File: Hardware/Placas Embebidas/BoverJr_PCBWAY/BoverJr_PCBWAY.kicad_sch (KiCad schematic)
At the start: 38 parts, among them J3 Encoder Derecho, J3 Programador, J4 Encoder Izquierdo, J5 Distancia_Der, J6 Distancia_Izq, J7 Distancia_Frontal, J8 7.4v, SW1 SW_Push, SW1 SW_SPDT, U1 ESP32-WROOM-32E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

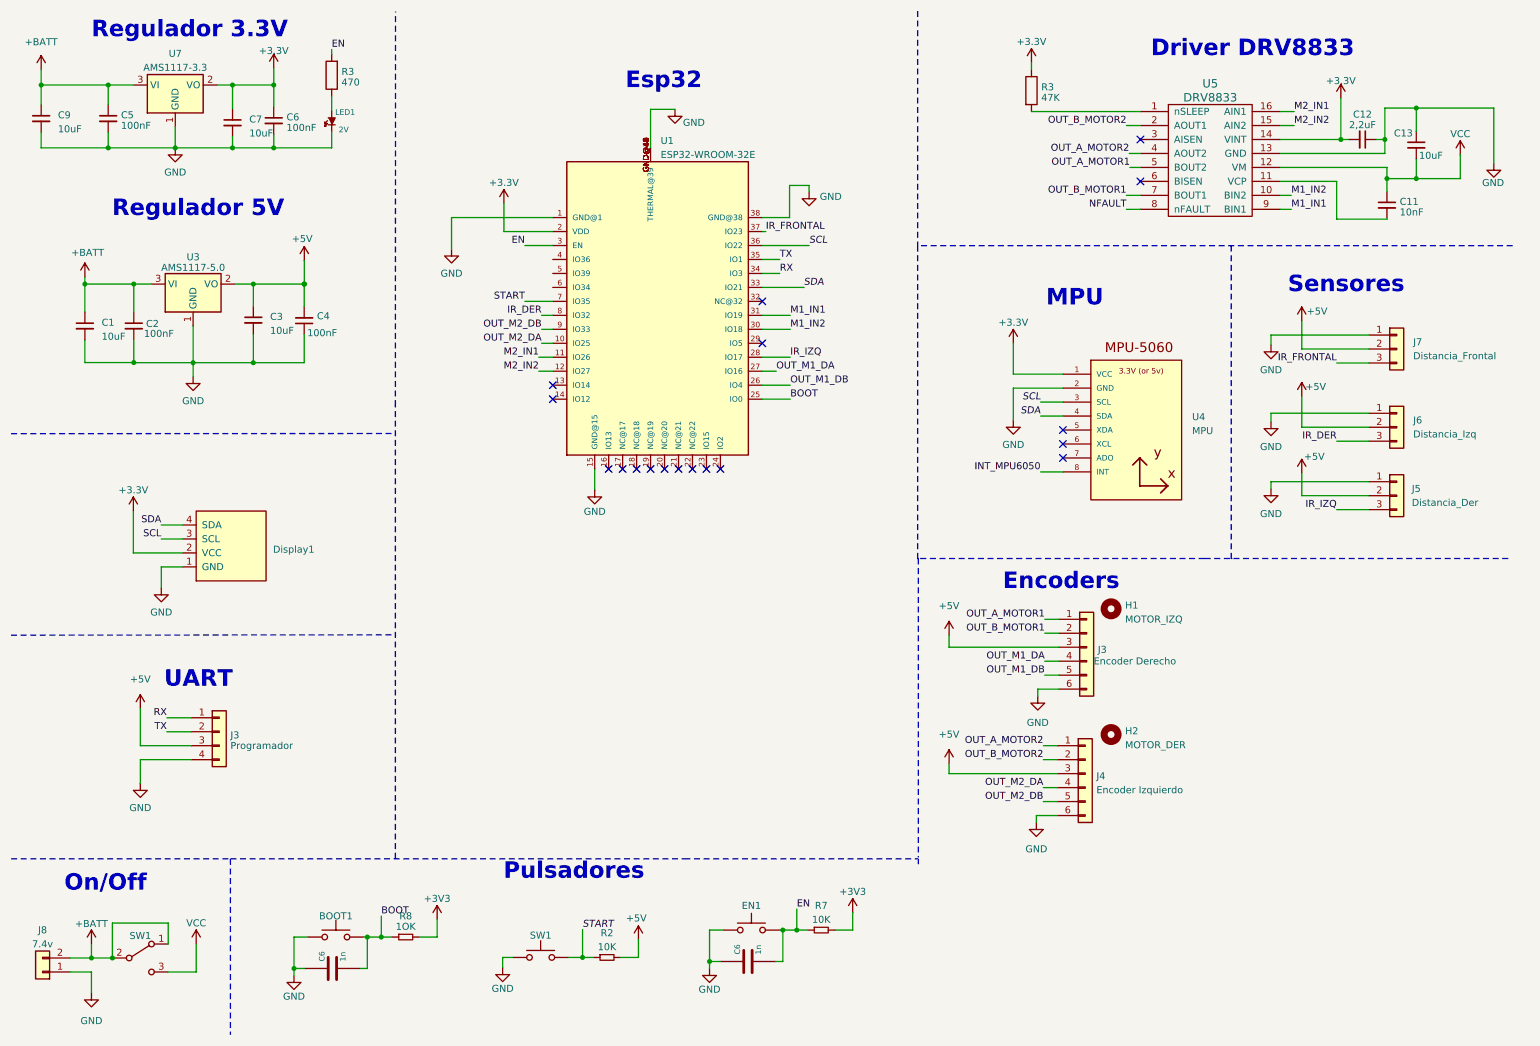
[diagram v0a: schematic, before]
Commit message: Placa falta verificar sch nuevamente , el 3d y los empaquetados de componentes quevamos a usar
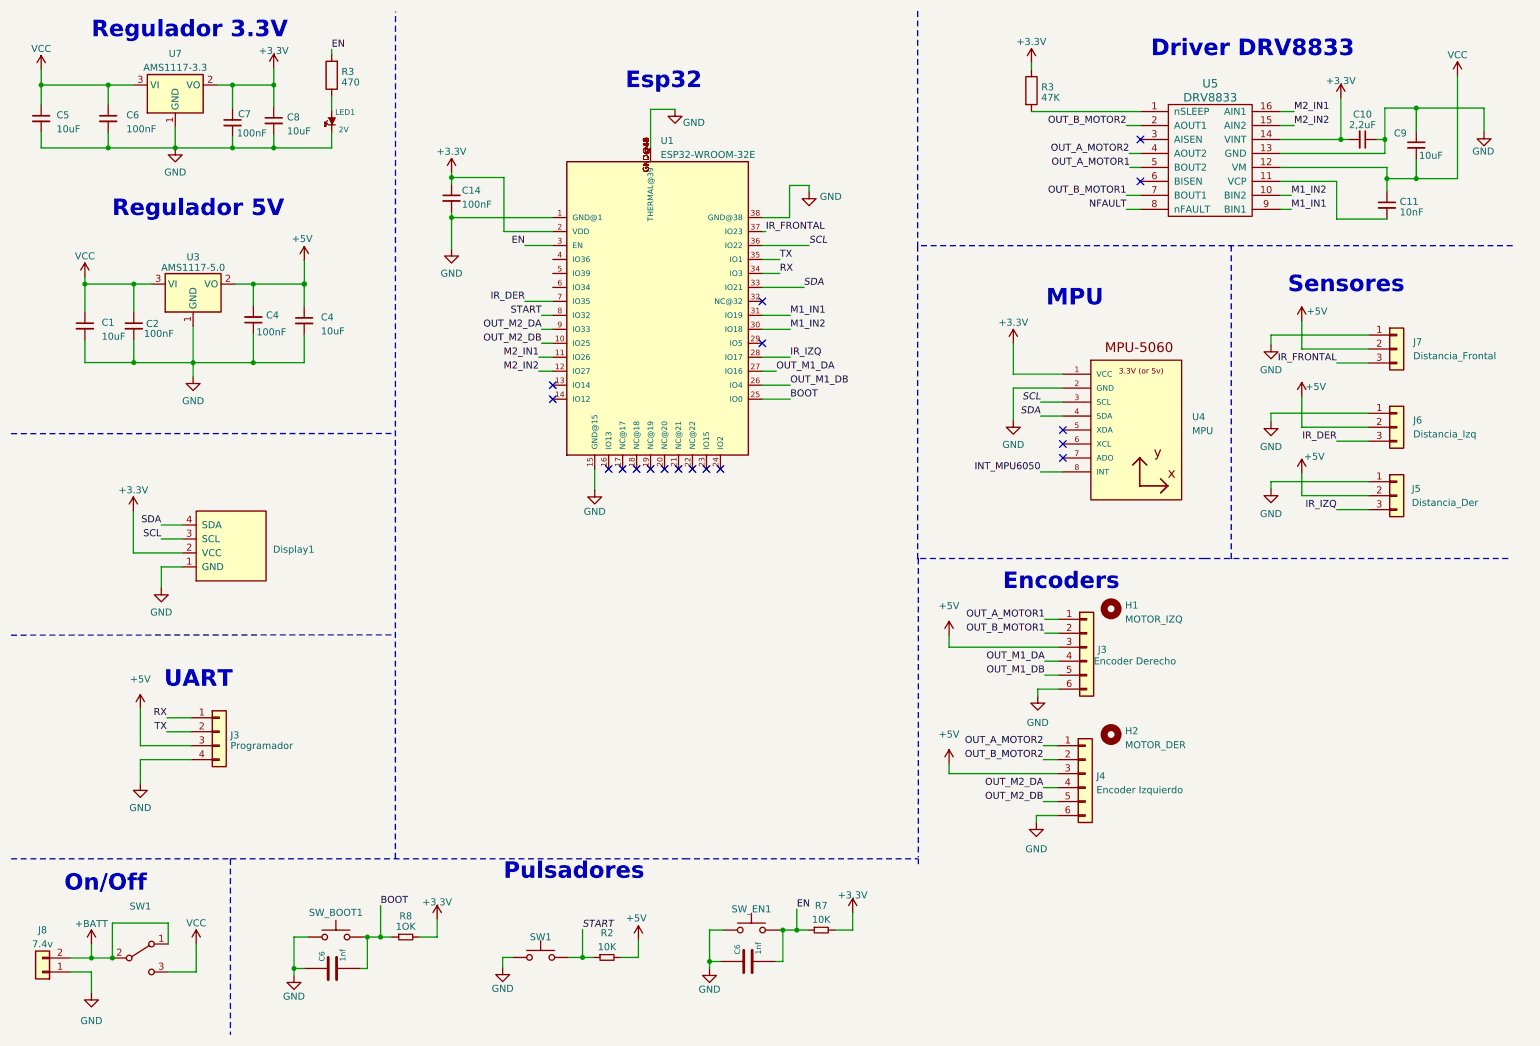
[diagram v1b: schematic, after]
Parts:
- removed C3: 10uF, EESTN5:C_1206, symbol Device:C_Small
- removed C4: 100nF, EESTN5:C_1206, symbol Device:C_Small
- added C14, C4: 100nF, Capacitor_SMD:C_0805_2012Metric, symbol Device:C_Small
- added C4: 10uF, Capacitor_SMD:C_0805_2012Metric, symbol Device:C_Small
- C1, C11, C2: footprint EESTN5:C_1206 -> Capacitor_SMD:C_0805_2012Metric
- C10: renamed from C12; footprint EESTN5:C_1206 -> Capacitor_SMD:C_0805_2012Metric
- C5: renamed from C9; footprint EESTN5:C_1206 -> Capacitor_SMD:C_0805_2012Metric
- C6: value 1n -> 1nf; footprint EESTN5:C_1206 -> Capacitor_SMD:C_0805_2012Metric
- C6: renamed from C5; footprint EESTN5:C_1206 -> Capacitor_SMD:C_0805_2012Metric
- C7: value 10uF -> 100nF; footprint EESTN5:C_1206 -> Capacitor_SMD:C_0805_2012Metric
- C8: renamed from C6; value 100nF -> 10uF; footprint EESTN5:C_1206 -> Capacitor_SMD:C_0805_2012Metric
- C9: renamed from C13; footprint EESTN5:C_1206 -> Capacitor_SMD:C_0805_2012Metric
- renumbered BOOT1 to SW_BOOT1, EN1 to SW_EN1
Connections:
- net +3V3 is gone; now on net +3.3V: R7.2, R8.2
- net +3.3V: now also C14.1
- net +5V: now also C4.1, C4.2
- net +BATT: no longer C1.1, C2.1, C5.1, C6.1, U3.3 (VI), U7.3 (VI)
- net GND: now also C14.2, C4.1, C4.2
- net IR_DER: now also U1.7 (IO35); no longer U1.8 (IO32)
- net OUT_M2_DA: now also U1.9 (IO33); no longer U1.10 (IO25)
- net OUT_M2_DB: now also U1.10 (IO25); no longer U1.9 (IO33)
- net START: now also U1.8 (IO32); no longer U1.7 (IO35)
- net VCC: now also C1.1, C2.1, C5.1, C6.1, U3.3 (VI), U7.3 (VI)

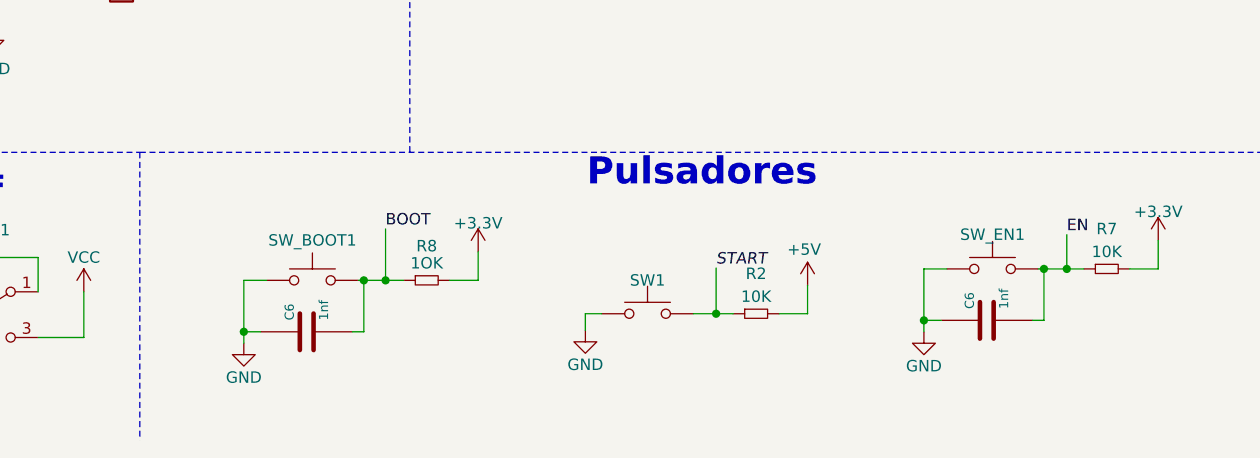
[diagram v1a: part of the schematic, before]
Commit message: FALTA VER EL TEMA DE LOS MOTORES SI SE PUEDE ACHICAR, ACOMODAR SERIGRAFIA Y AÑADIR LOGOS Y VERIFICAR X 3D , Y VER SI PODEMOS PONER JST
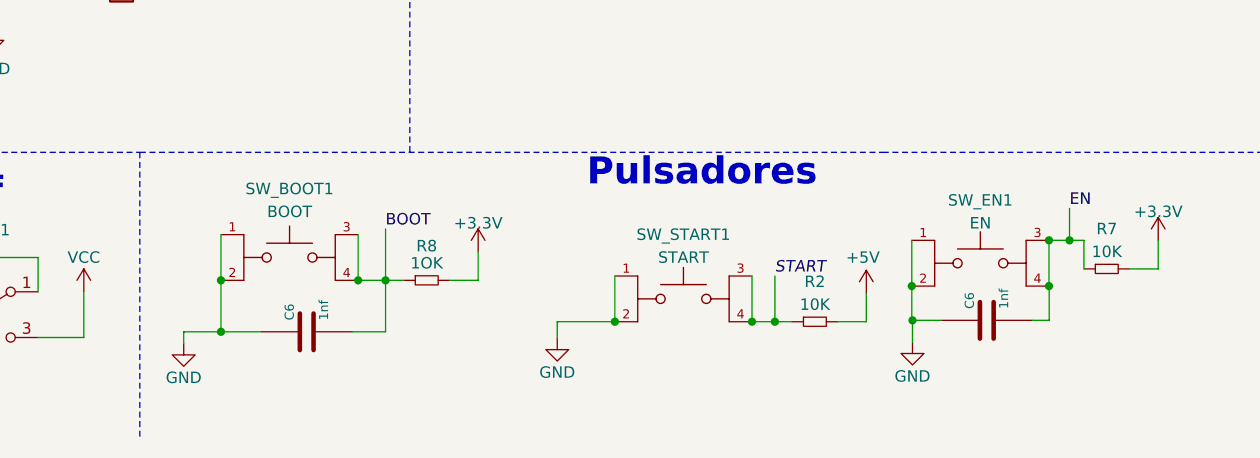
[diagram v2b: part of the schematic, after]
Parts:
- removed SW1: SW_Push, EESTN5:PUSH_SWITCH_THT, symbol EESTN5:SW_Push
- removed SW_BOOT1, SW_EN1: SW_Push, Diode_SMD:D_1206_3216Metric, symbol EESTN5:SW_Push
- added SW_BOOT1: BOOT, SW_TL3301FF160QG, symbol switch smd 6mm:TL3301FF160QG
- added SW_EN1: EN, SW_TL3301FF160QG, symbol switch smd 6mm:TL3301FF160QG
- added SW_START1: START, SW_TL3301FF160QG, symbol switch smd 6mm:TL3301FF160QG
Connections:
- net BOOT: now also SW_BOOT1.3, SW_BOOT1.4
- net EN: now also SW_EN1.3, SW_EN1.4
- net GND: now also SW_BOOT1.1, SW_BOOT1.2, SW_EN1.1, SW_EN1.2, SW_START1.1, SW_START1.2
- net START: now also SW_START1.3, SW_START1.4
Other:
- moved on the sheet: R2

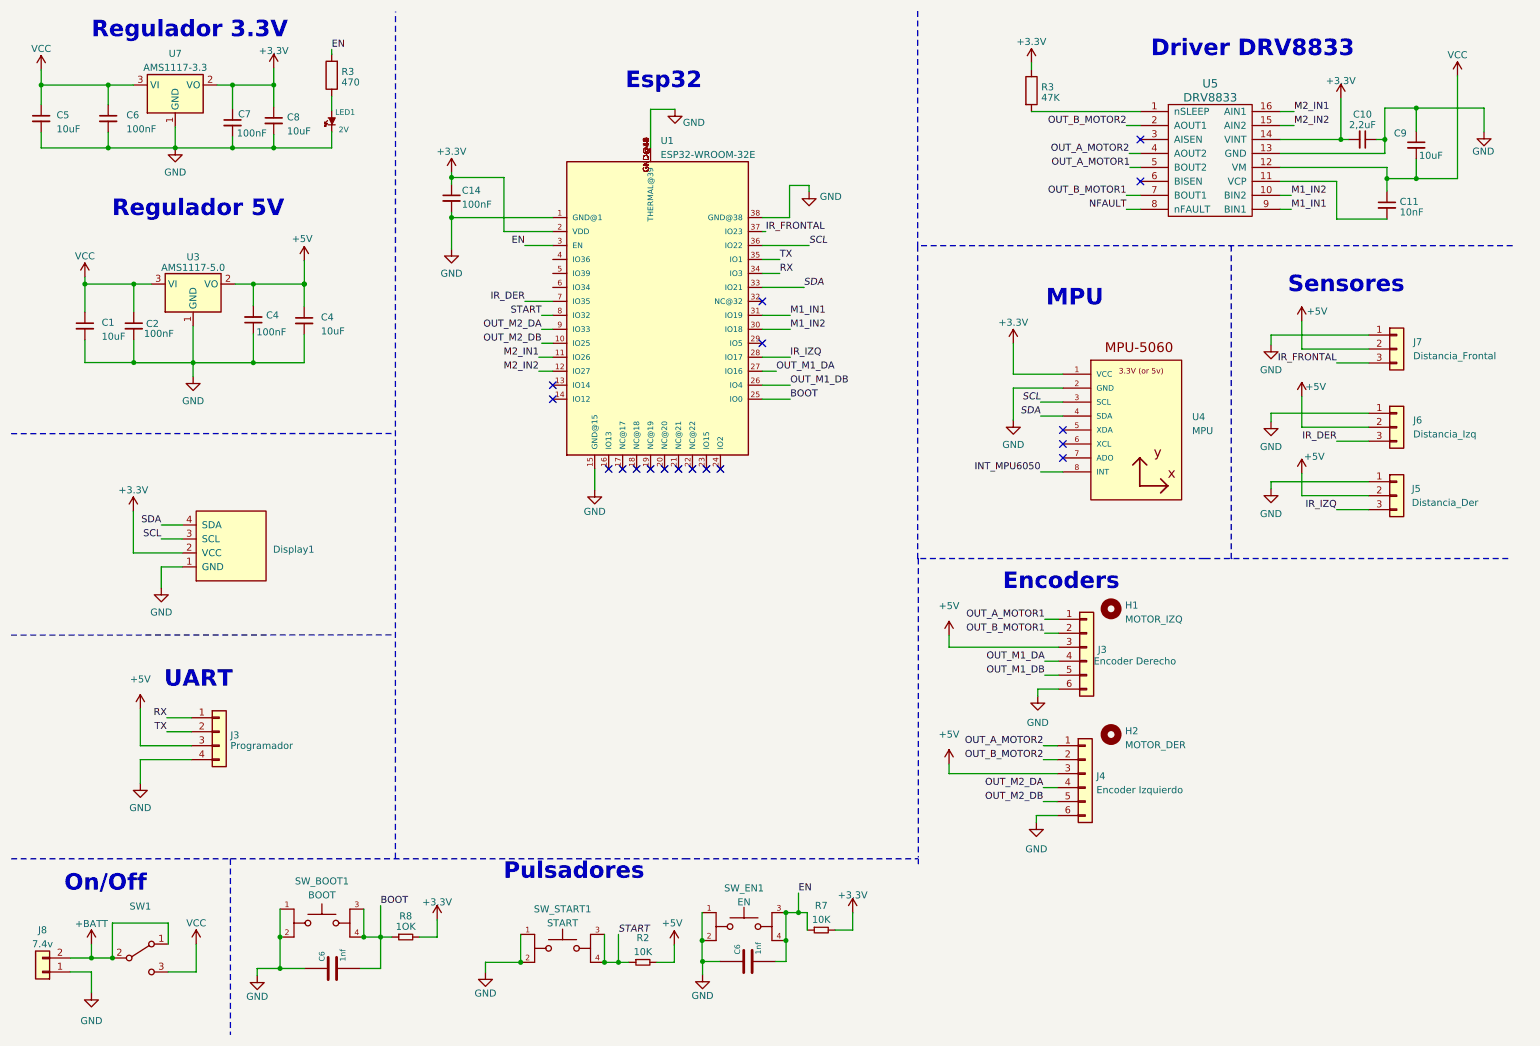
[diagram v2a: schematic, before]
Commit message: agregue logos , acomode serigrafia y componentes , agregue pads
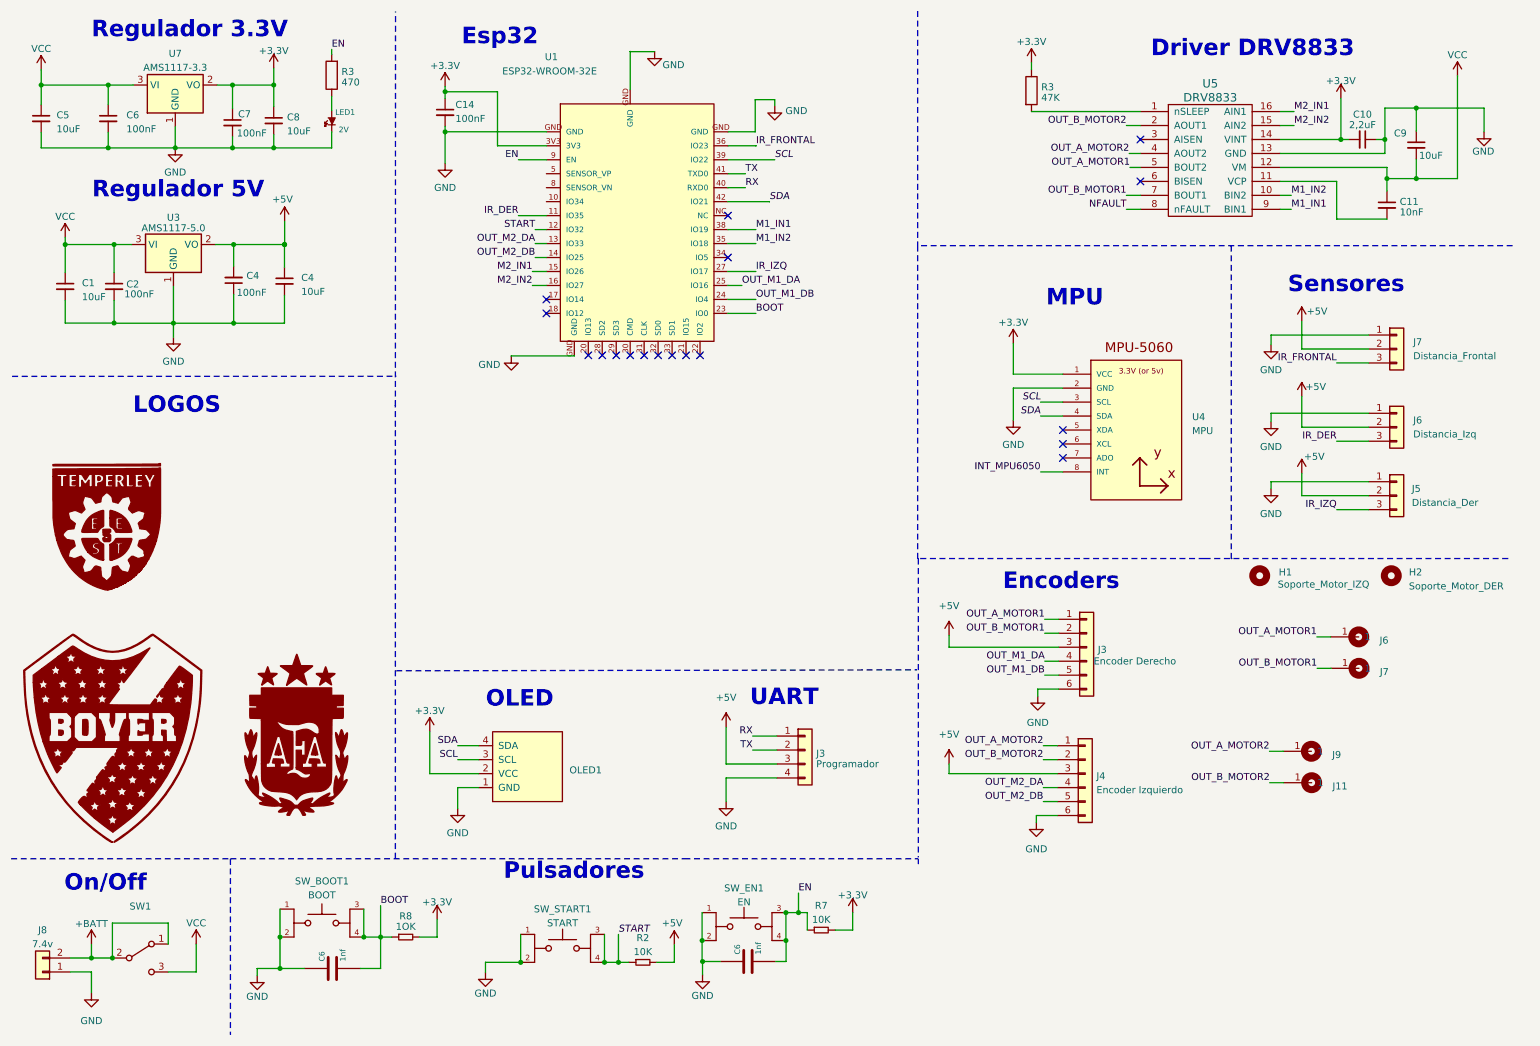
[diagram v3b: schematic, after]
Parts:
- removed Display1: SSD1306-SSD1306-128x64_OLED, EESTN5:128x64OLED, symbol EESTN5:SSD1306-SSD1306-128x64_OLED
- removed U1: ESP32-WROOM-32E, ESP32-WROOM-32E:ESP32-WROOM-32E, symbol ESP32-WROOM-32E:ESP32-WROOM-32E
- added G1: LOGO_EESTN5_2, EESTN5:EESTN5, symbol EESTN5:LOGO_EESTN5_2
- added G2: LOGO, EESTN5:Bover_huella_frontal, symbol Bover_Logo:LOGO
- added G3: LOGO, EESTN5:AFA, symbol AFA:LOGO
- added J11, J6, J7, J9: Cable_PAD, EESTN5:Cable_Doble_1,5mm, symbol EESTN5:Cable_PAD
- added OLED1: SSD1306-SSD1306-128x64_OLED, EESTN5:128x64OLED, symbol EESTN5:SSD1306-SSD1306-128x64_OLED
- added U1: ESP32-WROOM-32E, EESTN5:ESP32-WROOM-32E, symbol Librerias:ESP32-WROOM-32E
- H1: value MOTOR_IZQ -> Soporte_Motor_IZQ
- H2: value MOTOR_DER -> Soporte_Motor_DER
- SW_BOOT1, SW_EN1, SW_START1: footprint SW_TL3301FF160QG -> EESTN5:SW_TL3301FF160QG
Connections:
- net +3.3V: now also OLED1.2 (VCC), U1.3V3
- net BOOT: now also U1.23 (IO0)
- net EN: now also U1.9 (EN)
- net GND: now also OLED1.1 (GND), U1.GND
- net IR_DER: now also U1.11 (IO35)
- net IR_FRONTAL: now also U1.36 (IO23)
- net IR_IZQ: now also U1.27 (IO17)
- net M1_IN1: now also U1.38 (IO19)
- net M1_IN2: now also U1.35 (IO18)
- net M2_IN1: now also U1.15 (IO26)
- net M2_IN2: now also U1.16 (IO27)
- net OUT_A_MOTOR1: now also J6.1
- net OUT_A_MOTOR2: now also J9.1
- net OUT_B_MOTOR1: now also J7.1
- net OUT_B_MOTOR2: now also J11.1
- net OUT_M1_DA: now also U1.25 (IO16)
- net OUT_M1_DB: now also U1.24 (IO4)
- net OUT_M2_DA: now also U1.13 (IO33)
- net OUT_M2_DB: now also U1.14 (IO25)
- net RX: now also U1.40 (RXD0)
- net SCL: now also OLED1.3 (SCL), U1.39 (IO22)
- net SDA: now also OLED1.4 (SDA), U1.42 (IO21)
- net START: now also U1.12 (IO32)
- net TX: now also U1.41 (TXD0)
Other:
- note added: "LOGOS"
- note added: "OLED"
- moved on the sheet: C1, C14, C2, C4, H1, H2, U3
